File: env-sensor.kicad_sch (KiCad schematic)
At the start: 7 parts, among them U1401 BME280

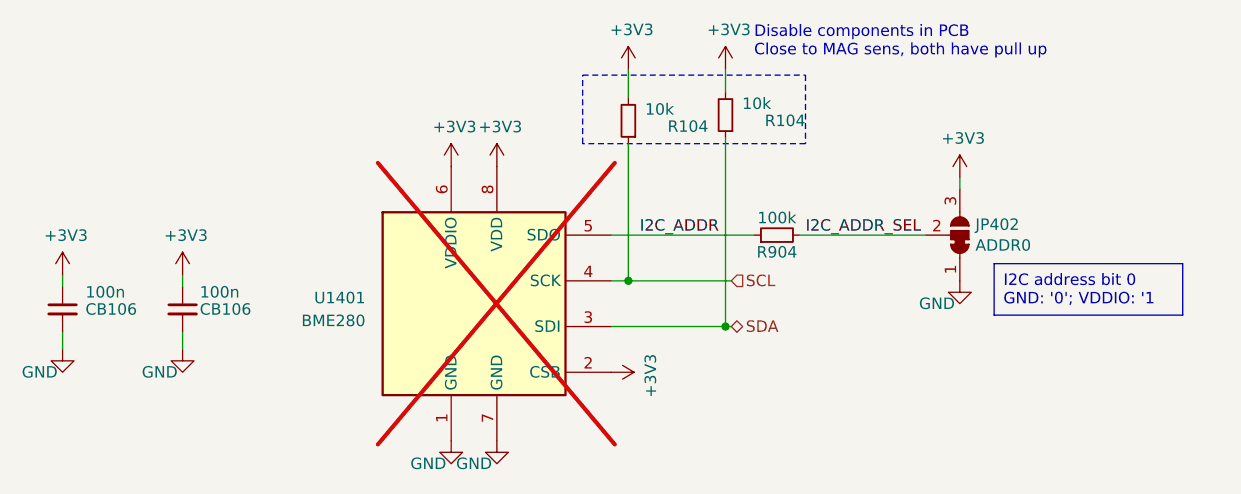
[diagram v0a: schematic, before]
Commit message: (pcb) route MAG & ENV sens.
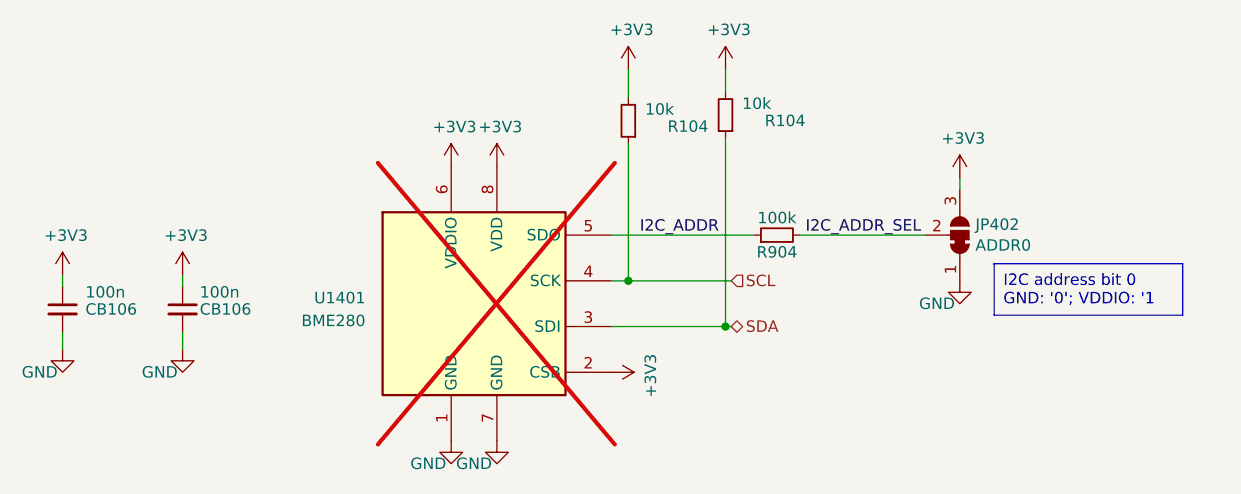
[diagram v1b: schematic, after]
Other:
- note removed: "Disable components in PCB Close to MAG sens, both have pull up"
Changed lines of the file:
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@@
     (stroke (width 0) (type default))
-  )
-  (rectangle (start 96.52 65.405) (end 121.285 73.025)
-    (stroke (width 0) (type dash))
-    (fill (type none))
   )
   (text_box "I2C address bit 0\nGND: '0'; VDDIO: '1"
@@
     (effects (font (size 1.27 1.27)) (justify left top))
   )
-  (text "Disable components in PCB\nClose to MAG sens, both have pull up"
-    (at 115.57 63.5 0)
-    (effects (font (size 1.27 1.27)) (justify left bottom))
-  )
   (label "I2C_ADDR" (at 102.87 83.185 0) (fields_autoplaced)
     (effects (font (size 1.27 1.27)) (justify left bottom))
@@
         )
         (path "/4185c36c-c66e-4dbd-be5d-841e551f4885/6761cd4a-72b1-4e84-88a1-1fb4245924b8"
-          (reference "#R1402") (unit 1)
+          (reference "R1402") (unit 1)
         )
       )
@@
         )
         (path "/4185c36c-c66e-4dbd-be5d-841e551f4885/6761cd4a-72b1-4e84-88a1-1fb4245924b8"
-          (reference "#R1401") (unit 1)
-        )
-      )
+          (reference "R1401") (unit 1)
+        )
+      )

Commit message: (sch) consoldate BOM
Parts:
- U1401: MPN (none) -> BME280; Mfr. (none) -> Bosch Sensortec
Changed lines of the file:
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@@
+      (effects (font (size 1.27 1.27)) hide)
+    )
+    (property "MPN" "BME280" (at 84.455 90.805 0)
+      (effects (font (size 1.27 1.27)) hide)
+    )
+    (property "Mfr." "Bosch Sensortec" (at 84.455 90.805 0)
       (effects (font (size 1.27 1.27)) hide)
     )

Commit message: (sch) clean up items for BOM
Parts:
- U1401: now fitted; now in the parts list
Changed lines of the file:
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@@
   )
   (symbol (lib_id "Sensor:BME280") (at 84.455 90.805 0) (unit 1)
-    (in_bom no) (on_board yes) (dnp yes) (fields_autoplaced)
+    (in_bom yes) (on_board yes) (dnp no) (fields_autoplaced)
     (property "Reference" "U1401" (at 72.39 90.17 0)
       (effects (font (size 1.27 1.27)) (justify right))

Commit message: (sch) exclude mounting holes & JP from BOM
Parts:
- JP402: now left out of the parts list
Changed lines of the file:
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@@
   )
   (symbol (lib_id "Jumper:SolderJumper_3_Bridged12") (at 138.43 83.185 270) (mirror x) (unit 1)
-    (in_bom yes) (on_board yes) (dnp no)
+    (in_bom no) (on_board yes) (dnp no)
     (property "Reference" "JP402" (at 140.1572 82.0166 90)
       (effects (font (size 1.27 1.27)) (justify left))
@@
       (effects (font (size 1.27 1.27)) hide)
     )
+    (property "MPN" "" (at 138.43 83.185 0)
+      (effects (font (size 1.27 1.27)) hide)
+    )
+    (property "Mfr." "" (at 138.43 83.185 0)
+      (effects (font (size 1.27 1.27)) hide)
+    )

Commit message: chore: update kicad version
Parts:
- renumbered CB106 to CB1409, CB106 to CB1410, JP402 to JP1401, R104 to R1401, R104 to R1402, R904 to R1403
